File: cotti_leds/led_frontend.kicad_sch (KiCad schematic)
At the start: 6 parts, among them Q1 PMOS Kp=0.2A/V² |Vth|=0.8V, Q2 NMOS

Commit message: feat: cotti_leds first version
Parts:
- D1: footprint (none) -> LED_SMD:LED_0603_1608Metric_Pad1.05x0.95mm_HandSolder
- Q1: footprint (none) -> footprints:local_SOT-416
- Q2: footprint (none) -> Package_TO_SOT_SMD:SOT-23-3
- R10, R11: footprint (none) -> Resistor_SMD:R_0805_2012Metric_Pad1.20x1.40mm_HandSolder; Digikey (none) -> https://www.digikey.com/en/products/detail/stackpole-electr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; Digikey P/N (none) -> RMCF0805FG100KCT-ND; Mfr. (none) -> Stackpole Electronics Inc; Mfr. P/N (none) -> RMCF0805FG100K
- R9: footprint (none) -> Resistor_SMD:R_0805_2012Metric_Pad1.20x1.40mm_HandSolder; Digikey (none) -> https://www.digikey.com/en/products/detail/stackpole-electr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; Digikey P/N (none) -> RMCF0805FT22R0CT-ND; Mfr. (none) -> Stackpole Electronics Inc; Mfr. P/N (none) -> RMCF0805FT22R0
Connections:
- net GND: now also Q1.3 (D), Q2.2 (S); no longer Q1.1 (D), Q2.3 (S)
- net IO_H: now also Q2.1 (G); no longer Q2.2 (G)
- net IO_L: now also Q1.1 (G), Q2.3 (D); no longer Q1.2 (G), Q2.1 (D)
- net at D1.1 (K): now also Q1.2 (S); no longer Q1.3 (S)
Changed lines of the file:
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@@
 			)
 		)
-		(property "Footprint" ""
-			(at 151.13 88.9 0)
+		(property "Footprint" "footprints:local_SOT-416"
+			(at 147.32 63.246 0)
 			(effects
 				(font
@@
 		)
 		(property "Description" "MOSFET P-CH 20V 100MA EMT3F"
-			(at 146.05 86.36 0)
+			(at 148.844 58.674 0)
 			(effects
 				(font
@@
 		)
 		(property "Digikey" "https://www.digikey.com/en/products/detail/rohm-semiconductor/RE1C001ZPTL/5042784"
-			(at 146.05 86.36 0)
+			(at 148.59 54.864 0)
 			(effects
 				(font
@@
 		)
 		(property "Digikey P/N" "RE1C001ZPTLCT-ND"
-			(at 146.05 86.36 0)
+			(at 148.082 48.514 0)
 			(effects
 				(font
@@
 		)
 		(property "Mfr." "Rohm Semiconductor"
-			(at 146.05 86.36 0)
+			(at 148.844 52.07 0)
 			(effects
 				(font
@@
 		)
 		(property "Mfr. P/N" "RE1C001ZPTL"
-			(at 146.05 86.36 0)
+			(at 146.558 45.72 0)
 			(effects
 				(font
@@
 			)
 		)
-		(property "Footprint" ""
+		(property "Footprint" "Resistor_SMD:R_0805_2012Metric_Pad1.20x1.40mm_HandSolder"
 			(at 124.206 99.314 90)
 			(effects
@@
 			)
 		)
-		(property "Datasheet" "~"
+		(property "Datasheet" "https://www.seielect.com/catalog/SEI-RMCF_RMCP.pdf"
 			(at 123.19 99.06 0)
 			(effects
@@
 			)
 		)
-		(property "Description" "Resistor, US symbol"
+		(property "Description" "RES 100K OHM 1% 1/8W 0805"
+			(at 123.19 99.06 0)
+			(effects
+				(font
+					(size 1.27 1.27)
+				)
+				(hide yes)
+			)
+		)
+		(property "Digikey" "https://www.digikey.com/en/products/detail/stackpole-electronics-inc/RMCF0805FG100K/1712614"
+			(at 123.19 99.06 0)
+			(effects
+				(font
+					(size 1.27 1.27)
+				)
+				(hide yes)
+			)
+		)
+		(property "Digikey P/N" "RMCF0805FG100KCT-ND"
+			(at 123.19 99.06 0)
+			(effects
+				(font
+					(size 1.27 1.27)
+				)
+				(hide yes)
+			)
+		)
+		(property "Mfr." "Stackpole Electronics Inc"
+			(at 123.19 99.06 0)
+			(effects
+				(font
+					(size 1.27 1.27)
+				)
+				(hide yes)
+			)
+		)
+		(property "Mfr. P/N" "RMCF0805FG100K"
 			(at 123.19 99.06 0)
 			(effects
@@
 			)
 		)
-		(property "Footprint" ""
+		(property "Footprint" "Resistor_SMD:R_0805_2012Metric_Pad1.20x1.40mm_HandSolder"
 			(at 149.606 63.754 90)
 			(effects
@@
 			)
 		)
-		(property "Datasheet" "~"
+		(property "Datasheet" "https://www.seielect.com/catalog/SEI-RMCF_RMCP.pdf"
 			(at 148.59 63.5 0)
 			(effects
@@
 			)
 		)
-		(property "Description" "Resistor, US symbol"
+		(property "Description" "RES 22 OHM 1% 1/8W 0805"
+			(at 148.59 63.5 0)
+			(effects
+				(font
+					(size 1.27 1.27)
+				)
+				(hide yes)
+			)
+		)
+		(property "Digikey" "https://www.digikey.com/en/products/detail/stackpole-electronics-inc/RMCF0805FT22R0/1712862"
+			(at 148.59 63.5 0)
+			(effects
+				(font
+					(size 1.27 1.27)
+				)
+				(hide yes)
+			)
+		)
+		(property "Digikey P/N" "RMCF0805FT22R0CT-ND"
+			(at 148.59 63.5 0)
+			(effects
+				(font
+					(size 1.27 1.27)
+				)
+				(hide yes)
+			)
+		)
+		(property "Mfr." "Stackpole Electronics Inc"
+			(at 148.59 63.5 0)
+			(effects
+				(font
+					(size 1.27 1.27)
+				)
+				(hide yes)
+			)
+		)
+		(property "Mfr. P/N" "RMCF0805FT22R0"
 			(at 148.59 63.5 0)
 			(effects
@@
 			)
 		)
-		(property "Footprint" ""
+		(property "Footprint" "Resistor_SMD:R_0805_2012Metric_Pad1.20x1.40mm_HandSolder"
 			(at 138.176 63.754 90)
 			(effects
@@
 			)
 		)
-		(property "Datasheet" "~"
+		(property "Datasheet" "https://www.seielect.com/catalog/SEI-RMCF_RMCP.pdf"
 			(at 137.16 63.5 0)
 			(effects
@@
 			)
 		)
-		(property "Description" "Resistor, US symbol"
+		(property "Description" "RES 100K OHM 1% 1/8W 0805"
+			(at 137.16 63.5 0)
+			(effects
+				(font
+					(size 1.27 1.27)
+				)
+				(hide yes)
+			)
+		)
+		(property "Digikey" "https://www.digikey.com/en/products/detail/stackpole-electronics-inc/RMCF0805FG100K/1712614"
+			(at 137.16 63.5 0)
+			(effects
+				(font
+					(size 1.27 1.27)
+				)
+				(hide yes)
+			)
+		)
+		(property "Digikey P/N" "RMCF0805FG100KCT-ND"
+			(at 137.16 63.5 0)
+			(effects
+				(font
+					(size 1.27 1.27)
+				)
+				(hide yes)
+			)
+		)
+		(property "Mfr." "Stackpole Electronics Inc"
+			(at 137.16 63.5 0)
+			(effects
+				(font
+					(size 1.27 1.27)
+				)
+				(hide yes)
+			)
+		)
+		(property "Mfr. P/N" "RMCF0805FG100K"
 			(at 137.16 63.5 0)
 			(effects
@@
 			)
 		)
-		(property "Footprint" ""
-			(at 139.7 91.44 0)
+		(property "Footprint" "Package_TO_SOT_SMD:SOT-23-3"
+			(at 135.636 116.332 0)
 			(effects
 				(font
@@
 		)
 		(property "Description" "MOSFET, N-CH, SINGLE, 0.3A, 60V,"
-			(at 134.62 93.98 0)
+			(at 135.382 119.888 0)
 			(effects
 				(font
@@
 		)
 		(property "Digikey" "https://www.digikey.com/en/products/detail/good-ark-semiconductor/2N7002K/18667796"
-			(at 134.62 93.98 0)
+			(at 134.366 123.19 0)
 			(effects
 				(font
@@
 		)
 		(property "Digikey P/N" "4786-2N7002KCT-ND"
-			(at 134.62 93.98 0)
+			(at 135.128 129.032 0)
 			(effects
 				(font
@@
 		)
 		(property "Mfr." "Good-Ark Semiconductor"
-			(at 134.62 93.98 0)
+			(at 134.366 125.476 0)
 			(effects
 				(font
@@
 		)
 		(property "Mfr. P/N" "2N7002K"
-			(at 134.62 93.98 0)
+			(at 134.62 132.334 0)
 			(effects
 				(font
@@
 			)
 		)
-		(property "Footprint" ""
+		(property "Footprint" "LED_SMD:LED_0603_1608Metric_Pad1.05x0.95mm_HandSolder"
 			(at 148.59 73.66 0)
 			(effects

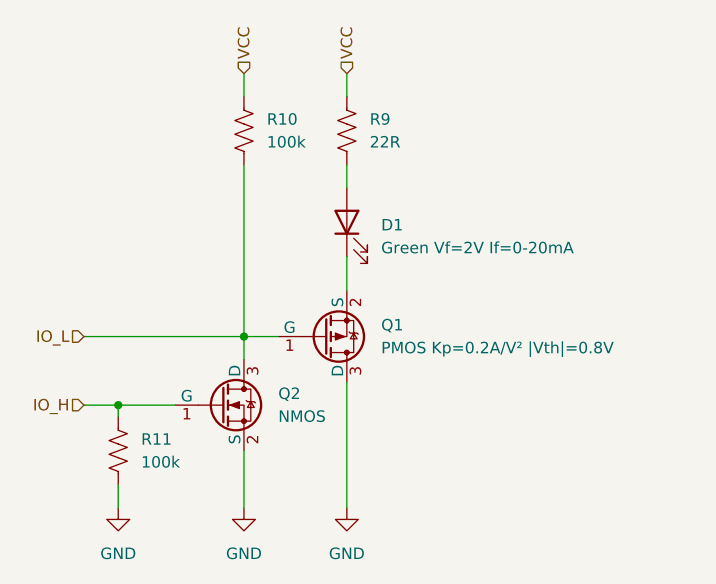
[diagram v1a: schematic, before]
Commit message: feat: cotti leds with new library format
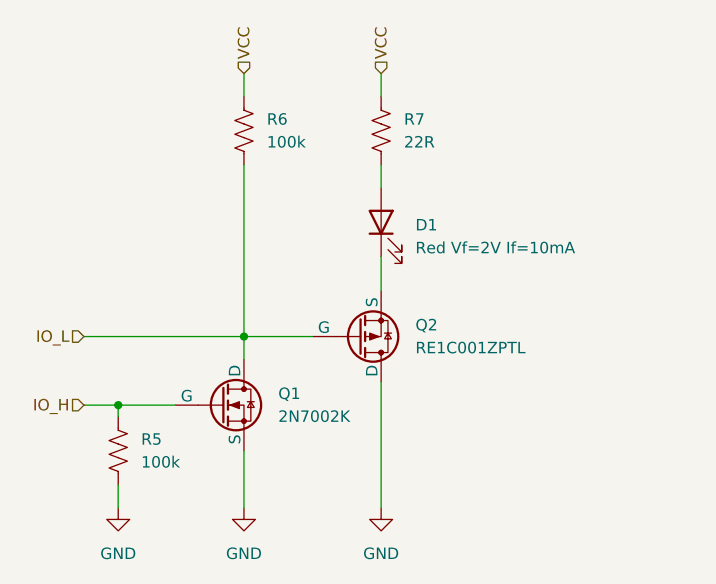
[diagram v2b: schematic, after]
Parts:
- removed D1: Green Vf=2V If=0-20mA, LED_SMD:LED_0603_1608Metric_Pad1.05x0.95mm_HandSolder, symbol Device:LED
- removed Q1: PMOS Kp=0.2A/V² |Vth|=0.8V, footprints:local_SOT-416, symbol Simulation_SPICE:PMOS
- removed Q2: NMOS, Package_TO_SOT_SMD:SOT-23-3, symbol Simulation_SPICE:NMOS
- added D1: Red Vf=2V If=10mA, LED_SMD:LED_0603_1608Metric_Pad1.05x0.95mm_HandSolder, symbol cotti_leds:LED_Red_SMD
- added Q1: 2N7002K, Package_TO_SOT_SMD:SOT-23-3, symbol cotti_transistors:2N7002K
- added Q2: RE1C001ZPTL, Package_TO_SOT_SMD:SOT-416, symbol cotti_transistors:RE1C001ZPTL
- R5: renamed from R11; Digikey P/N RMCF0805FG100KCT-ND -> (none)
- R6: renamed from R10; Digikey P/N RMCF0805FG100KCT-ND -> (none)
- R7: renamed from R9; Digikey P/N RMCF0805FT22R0CT-ND -> (none)
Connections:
- net GND: now also Q1.2 (S), Q2.3 (D)
- net IO_H: now also Q1.1 (G)
- net IO_L: now also Q1.3 (D), Q2.1 (G)
- net at R7.2: now also D1.2 (A)
- new net: D1.1 (K), Q2.2 (S)
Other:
- moved on the sheet: R7

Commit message: feat: cotti leds gerber files
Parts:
- Q2: footprint Package_TO_SOT_SMD:SOT-416 -> cotti_footprints:SOT-416
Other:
- company: (none) -> Cotti
- title: (none) -> Led module
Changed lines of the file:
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@@
 	(generator_version "9.0")
 	(paper "A4")
+	(title_block
+		(title "Led module")
+		(date "2026-01-17")
+		(rev "0.0")
+		(company "Cotti")
+	)
 	(junction
 		(at 137.16 86.36)
@@
 			)
 		)
-		(property "Footprint" "Package_TO_SOT_SMD:SOT-416"
+		(property "Footprint" "cotti_footprints:SOT-416"
 			(at 149.606 49.276 0)
 			(effects
